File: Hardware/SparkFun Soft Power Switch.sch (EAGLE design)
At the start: 32 parts, among them J1 Ext Button, J6 MCU Control, J7 System Power, Q1 DMC2700UDM

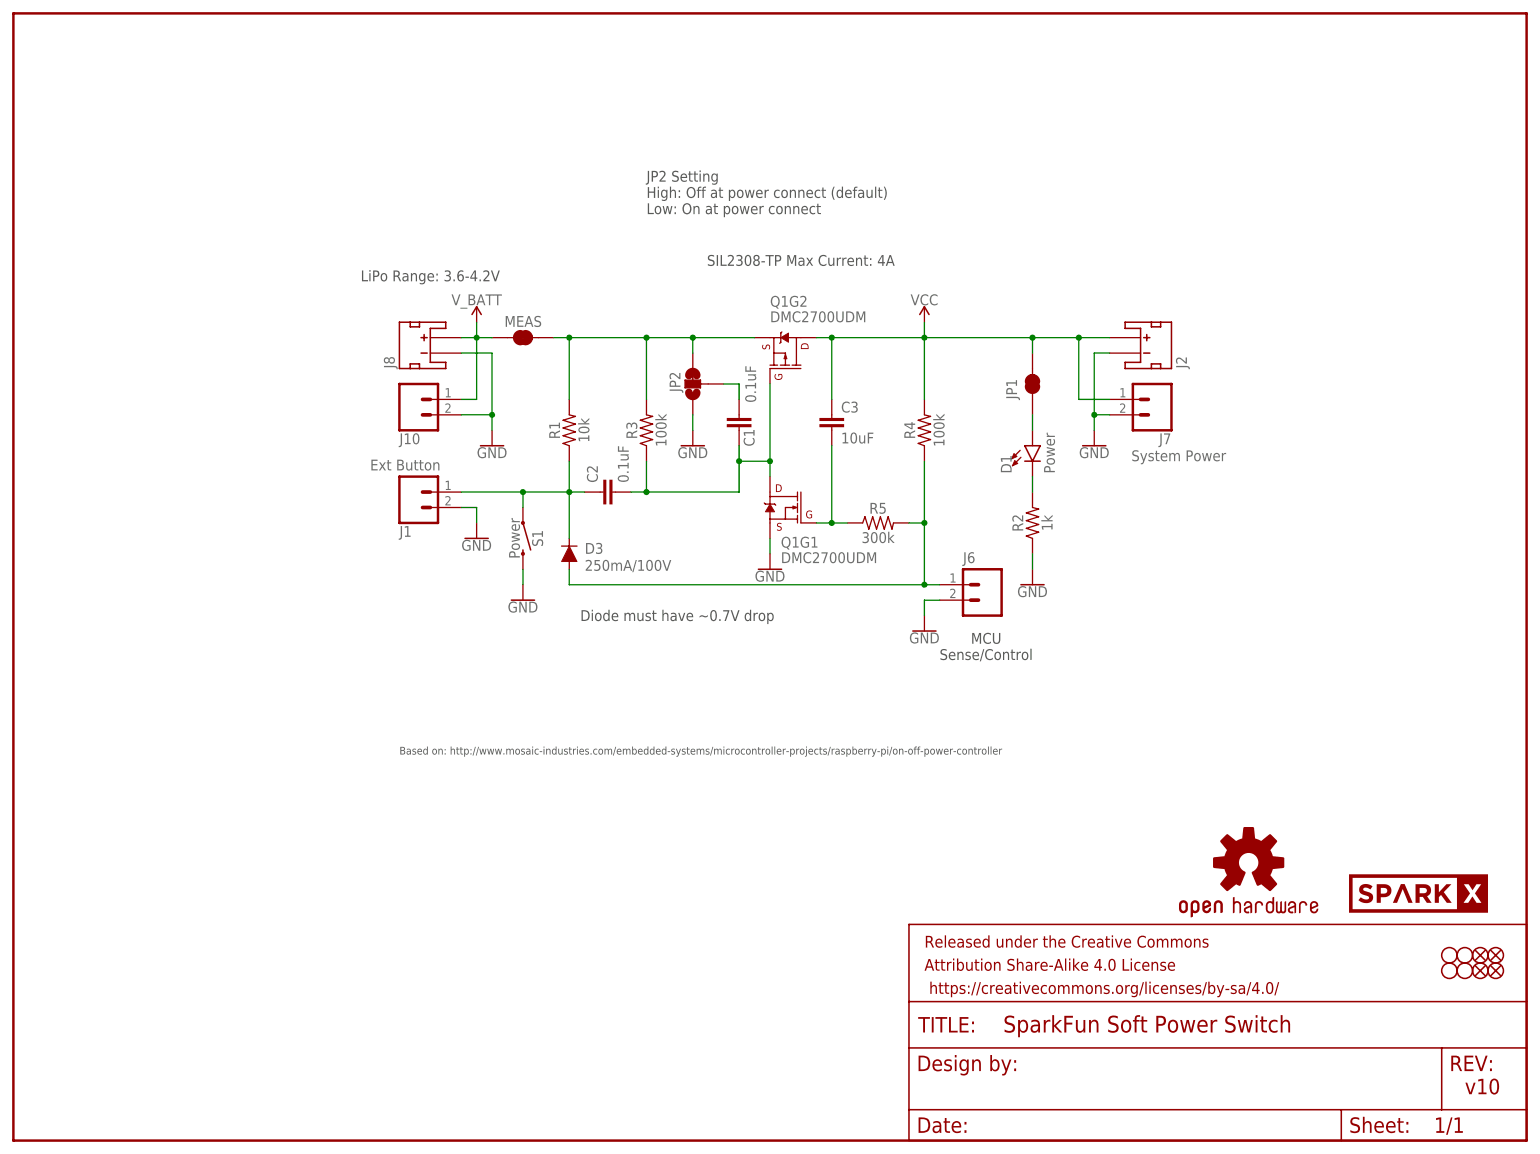
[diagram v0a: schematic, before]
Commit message: x02: Add fast off. Add zener protection. Increase V rating of cap. Increase cap size.
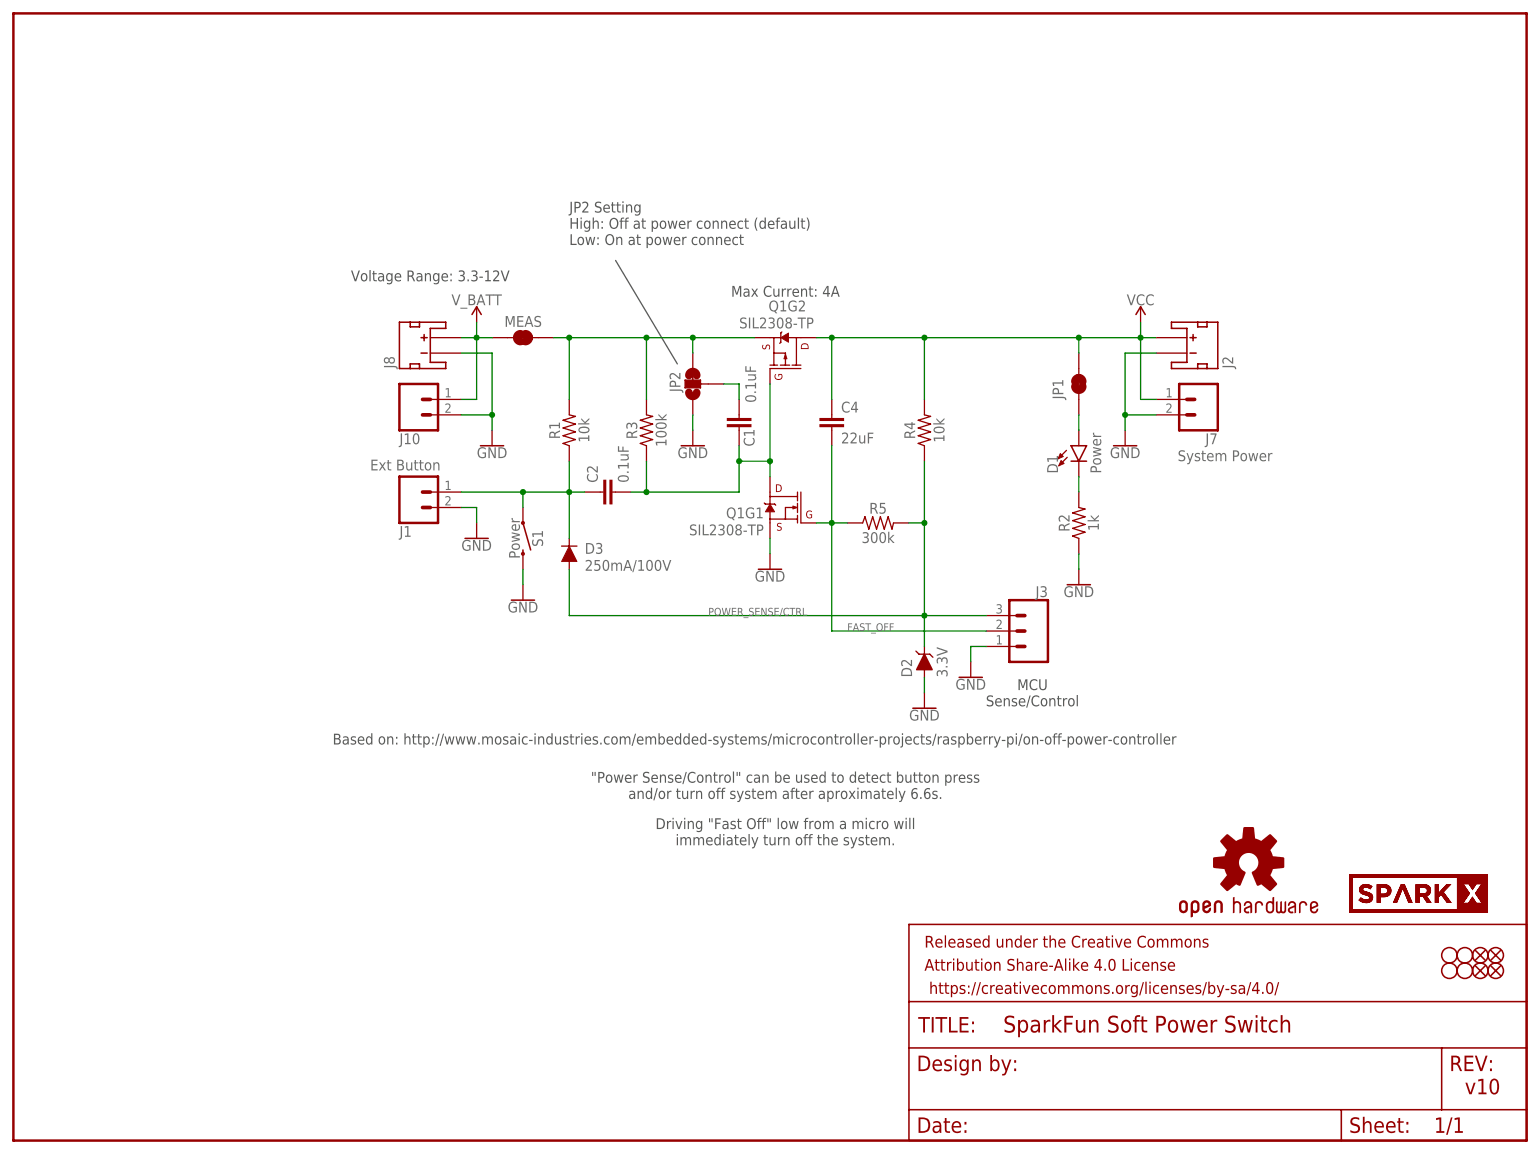
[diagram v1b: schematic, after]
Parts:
- removed C3: 10uF, SparkFun-Capacitors:10UF-0603-6.3V-20%
- removed J6: MCU Control, SparkFun-Connectors:CONN_021X02_NO_SILK
- added C4: 22uF, SparkFun-Capacitors:22UF-0805-16V-20%
- added D2: 3.3V, SparkFun-DiscreteSemi:DIODE-ZENER-MM3Z3V3T1G
- added J3: (no value), SparkFun-Connectors:CONN_031X03_NO_SILK
- added U$15: SPARKX-LOGO2, SparkX:SPARKX-LOGO2
- Q1: value DMC2700UDM -> SIL2308-TP; device SparkFun-DiscreteSemi:MOSFET_COMPLIMENTARY_PAIR-DMC2700UDM -> SparkFun-DiscreteSemi:MOSFET_COMPLIMENTARY_PAIR-SIL2308
- R4: value 100k -> 10k; device SparkFun-Resistors:100KOHM-0603-1/10W-1% -> SparkFun-Resistors:10KOHM-0603-1/10W-1%
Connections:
- removed net N$8: C3.2, Q1G1.G, R5.1
- new net FAST_OFF: C4.2, J3.2, Q1G1.G, R5.1
- net GND: now also D2.A, J3.1; no longer J6.2
- net POWER_SENSE/CTRL: now also D2.C, J3.3; no longer J6.1
- net VCC: now also C4.1; no longer C3.1
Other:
- note added: ""Power Sense/Control" can be used to detect button press and/or turn off system after aproximately 6.6s."
- note added: "Driving "Fast Off" low from a micro will immediately turn off the system."
- note added: "Max Current: 4A"
- note added: "Voltage Range: 3.3-12V"
- note removed: "Diode must have ~0.7V drop"
- note removed: "LiPo Range: 3.6-4.2V"
- note removed: "SIL2308-TP Max Current: 4A"
- moved on the sheet: D1, J2, J7, JP1, R2
